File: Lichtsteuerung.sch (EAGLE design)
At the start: 132 parts, among them IC1 74HC595D, IC10 TSR_1-2450, IC11 MEGA64-A, IC12 75176AD, IC13 DS1307SO8, IC2 74HC595D, IC3 74HC595D, IC4 74HC595D, IC5 75176AD, IC6 MEGA8-AI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

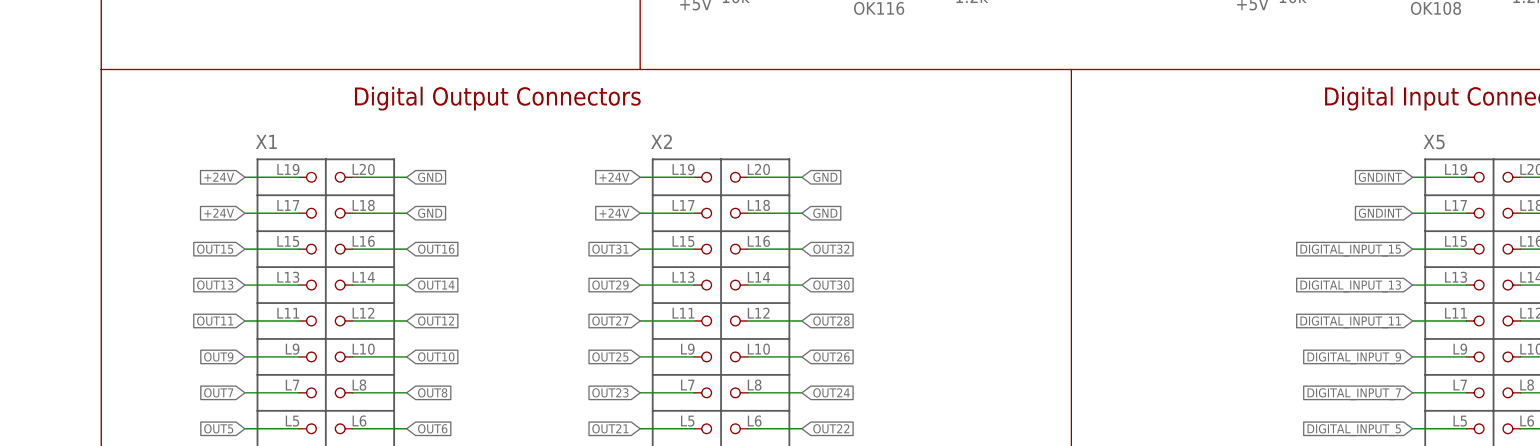
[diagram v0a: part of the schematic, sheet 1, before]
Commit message: Added polyfuses for the 24V rails
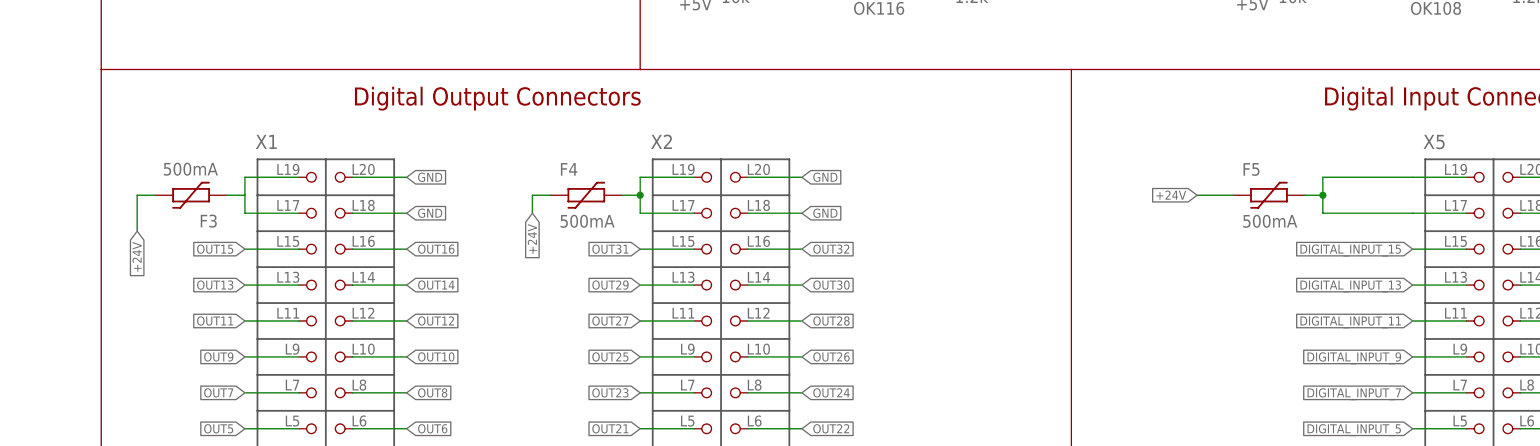
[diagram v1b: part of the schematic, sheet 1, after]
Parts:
- added F3, F4, F5: 500mA, ptc-littlefuse:1812L
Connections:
- new net +24V_01: F3.1, X1.L17, X1.L19
- new net +24V_02: F4.2, X2.L17, X2.L19
- new net +24V_03: F5.2, X5.L17, X5.L19
- net +24V: now also F3.2, F4.1, F5.1; no longer X1.L17, X1.L19, X2.L17, X2.L19
- net GNDINT: no longer X5.L17, X5.L19
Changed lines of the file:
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@@
 <part name="L2" library="epcos-b82790c0" deviceset="EPCOS_B82790C0" device="" value="2x51µH"/>
 <part name="JP3" library="pinhead" deviceset="PINHD-2X8" device=""/>
+<part name="F3" library="ptc-littlefuse" deviceset="1812L" device="" value="500mA"/>
+<part name="F4" library="ptc-littlefuse" deviceset="1812L" device="" value="500mA"/>
+<part name="F5" library="ptc-littlefuse" deviceset="1812L" device="" value="500mA"/>
 </parts>
 <sheets>
@@
 <instance part="P+26" gate="1" x="220.98" y="124.46" rot="R90"/>
 <instance part="P+27" gate="1" x="220.98" y="106.68" rot="R90"/>
+<instance part="F3" gate="G$1" x="152.4" y="76.2" rot="R180"/>
+<instance part="F4" gate="G$1" x="208.28" y="76.2"/>
+<instance part="F5" gate="G$1" x="304.8" y="76.2"/>
 </instances>
 <busses>
@@
 </segment>
 <segment>
-<wire x1="167.64" y1="78.74" x2="160.02" y2="78.74" width="0.1524" layer="91"/>
-<label x="160.02" y="78.74" size="1.27" layer="95" rot="R180" xref="yes"/>
-<pinref part="X1" gate="G$1" pin="L19"/>
-</segment>
-<segment>
-<wire x1="167.64" y1="73.66" x2="160.02" y2="73.66" width="0.1524" layer="91"/>
-<label x="160.02" y="73.66" size="1.27" layer="95" rot="R180" xref="yes"/>
-<pinref part="X1" gate="G$1" pin="L17"/>
-</segment>
-<segment>
-<wire x1="223.52" y1="78.74" x2="215.9" y2="78.74" width="0.1524" layer="91"/>
-<label x="215.9" y="78.74" size="1.27" layer="95" rot="R180" xref="yes"/>
-<pinref part="X2" gate="G$1" pin="L19"/>
-</segment>
-<segment>
-<wire x1="223.52" y1="73.66" x2="215.9" y2="73.66" width="0.1524" layer="91"/>
-<label x="215.9" y="73.66" size="1.27" layer="95" rot="R180" xref="yes"/>
-<pinref part="X2" gate="G$1" pin="L17"/>
+<pinref part="F5" gate="G$1" pin="1"/>
+<wire x1="299.72" y1="76.2" x2="294.64" y2="76.2" width="0.1524" layer="91"/>
+<label x="294.64" y="76.2" size="1.27" layer="95" rot="R180" xref="yes"/>
+</segment>
+<segment>
+<pinref part="F4" gate="G$1" pin="1"/>
+<wire x1="203.2" y1="76.2" x2="200.66" y2="76.2" width="0.1524" layer="91"/>
+<wire x1="200.66" y1="76.2" x2="200.66" y2="73.66" width="0.1524" layer="91"/>
+<label x="200.66" y="73.66" size="1.27" layer="95" rot="R270" xref="yes"/>
+</segment>
+<segment>
+<pinref part="F3" gate="G$1" pin="2"/>
+<wire x1="147.32" y1="76.2" x2="144.78" y2="76.2" width="0.1524" layer="91"/>
+<wire x1="144.78" y1="76.2" x2="144.78" y2="71.12" width="0.1524" layer="91"/>
+<label x="144.78" y="71.12" size="1.27" layer="95" rot="R270" xref="yes"/>
 </segment>
 </net>
@@
 </segment>
 <segment>
-<wire x1="332.74" y1="78.74" x2="325.12" y2="78.74" width="0.1524" layer="91"/>
-<label x="325.12" y="78.74" size="1.27" layer="95" rot="R180" xref="yes"/>
-<pinref part="X5" gate="G$1" pin="L19"/>
-</segment>
-<segment>
-<wire x1="332.74" y1="73.66" x2="325.12" y2="73.66" width="0.1524" layer="91"/>
-<label x="325.12" y="73.66" size="1.27" layer="95" rot="R180" xref="yes"/>
-<pinref part="X5" gate="G$1" pin="L17"/>
-</segment>
-<segment>
 <wire x1="340.36" y1="78.74" x2="347.98" y2="78.74" width="0.1524" layer="91"/>
 <label x="347.98" y="78.74" size="1.27" layer="95" xref="yes"/>
@@
 </segment>
 </net>
+<net name="+24V_01" class="1">
+<segment>
+<wire x1="167.64" y1="78.74" x2="160.02" y2="78.74" width="0.1524" layer="91"/>
+<pinref part="X1" gate="G$1" pin="L19"/>
+<wire x1="167.64" y1="73.66" x2="160.02" y2="73.66" width="0.1524" layer="91"/>
+<pinref part="X1" gate="G$1" pin="L17"/>
+<wire x1="160.02" y1="78.74" x2="160.02" y2="76.2" width="0.1524" layer="91"/>
+<wire x1="160.02" y1="76.2" x2="160.02" y2="73.66" width="0.1524" layer="91"/>
+<wire x1="160.02" y1="76.2" x2="157.48" y2="76.2" width="0.1524" layer="91"/>
+<pinref part="F3" gate="G$1" pin="1"/>
+</segment>
+</net>
+<net name="+24V_02" class="1">
+<segment>
+<wire x1="223.52" y1="78.74" x2="215.9" y2="78.74" width="0.1524" layer="91"/>
+<pinref part="X2" gate="G$1" pin="L19"/>
+<pinref part="F4" gate="G$1" pin="2"/>
+<wire x1="213.36" y1="76.2" x2="215.9" y2="76.2" width="0.1524" layer="91"/>
+<wire x1="215.9" y1="76.2" x2="215.9" y2="78.74" width="0.1524" layer="91"/>
+<wire x1="223.52" y1="73.66" x2="215.9" y2="73.66" width="0.1524" layer="91"/>
+<pinref part="X2" gate="G$1" pin="L17"/>
+<wire x1="215.9" y1="76.2" x2="215.9" y2="73.66" width="0.1524" layer="91"/>
+<junction x="215.9" y="76.2"/>
+</segment>
+</net>
+<net name="+24V_03" class="1">
+<segment>
+<wire x1="332.74" y1="78.74" x2="325.12" y2="78.74" width="0.1524" layer="91"/>
+<pinref part="X5" gate="G$1" pin="L19"/>
+<pinref part="F5" gate="G$1" pin="2"/>
+<wire x1="309.88" y1="76.2" x2="312.42" y2="76.2" width="0.1524" layer="91"/>
+<wire x1="312.42" y1="76.2" x2="312.42" y2="78.74" width="0.1524" layer="91"/>
+<wire x1="312.42" y1="78.74" x2="325.12" y2="78.74" width="0.1524" layer="91"/>
+<wire x1="312.42" y1="76.2" x2="312.42" y2="73.66" width="0.1524" layer="91"/>
+<wire x1="332.74" y1="73.66" x2="325.12" y2="73.66" width="0.1524" layer="91"/>
+<pinref part="X5" gate="G$1" pin="L17"/>
+<wire x1="312.42" y1="73.66" x2="325.12" y2="73.66" width="0.1524" layer="91"/>
+<junction x="312.42" y="76.2"/>
+</segment>
+</net>

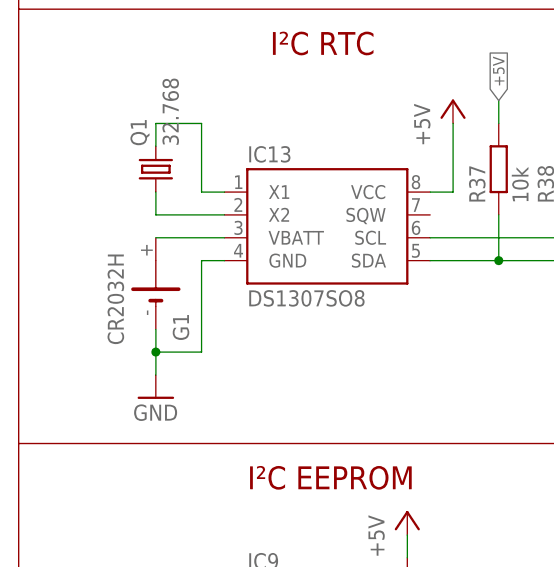
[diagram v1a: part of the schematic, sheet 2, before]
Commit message: Fixed wrong battery holder
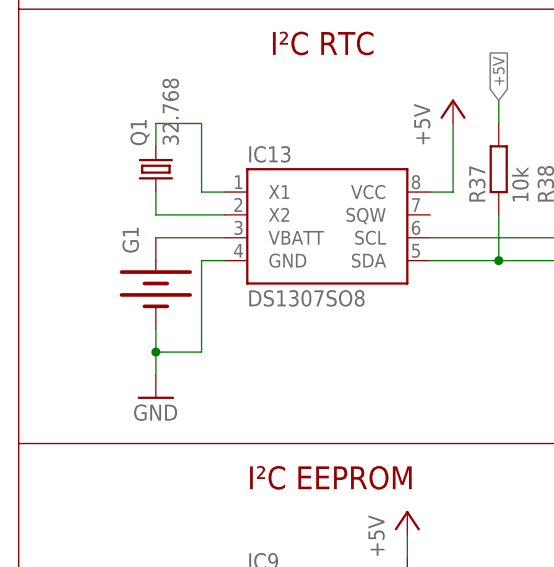
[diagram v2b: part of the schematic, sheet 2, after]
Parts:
- G1: value CR2032H -> (none); device battery:CR2032H -> SparkFun:BATTERY20PTH
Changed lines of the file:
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@@
 <part name="FRAME3" library="frames" deviceset="A3L-LOC" device=""/>
 <part name="IC13" library="SparkFun" deviceset="DS1307" device="SO8"/>
-<part name="G1" library="battery" deviceset="CR2032H" device=""/>
+<part name="G1" library="SparkFun" deviceset="BATTERY" device="20PTH"/>
 <part name="Q1" library="crystal" deviceset="MC-306" device="" value="32.768"/>
 <part name="R37" library="resistor" deviceset="R-EU_" device="R0805" value="10k"/>
@@
 <instance part="FRAME3" gate="G$1" x="0" y="0"/>
 <instance part="IC13" gate="G$1" x="43.18" y="147.32"/>
-<instance part="G1" gate="1" x="25.4" y="139.7" smashed="yes" rot="R90">
-<attribute name="NAME" x="27.305" y="136.398" size="1.778" layer="95" rot="R270"/>
-<attribute name="VALUE" x="21.844" y="132.842" size="1.778" layer="96" rot="R90"/>
+<instance part="G1" gate="G$1" x="25.4" y="139.7" smashed="yes" rot="R270">
+<attribute name="NAME" x="23.495" y="143.002" size="1.778" layer="95" rot="R90"/>
+<attribute name="VALUE" x="28.956" y="146.558" size="1.778" layer="96" rot="R270"/>
 </instance>
 <instance part="Q1" gate="P" x="25.4" y="152.4" rot="R90"/>
@@
 <segment>
 <wire x1="25.4" y1="144.78" x2="33.02" y2="144.78" width="0.1524" layer="91"/>
-<pinref part="G1" gate="1" pin="+"/>
+<pinref part="G1" gate="G$1" pin="+"/>
 <pinref part="IC13" gate="G$1" pin="VBATT"/>
 </segment>
@@
 <wire x1="25.4" y1="129.54" x2="25.4" y2="132.08" width="0.1524" layer="91"/>
 <junction x="25.4" y="132.08"/>
-<pinref part="G1" gate="1" pin="-"/>
+<pinref part="G1" gate="G$1" pin="-"/>
 <pinref part="IC13" gate="G$1" pin="GND"/>
 <pinref part="GND21" gate="1" pin="GND"/>

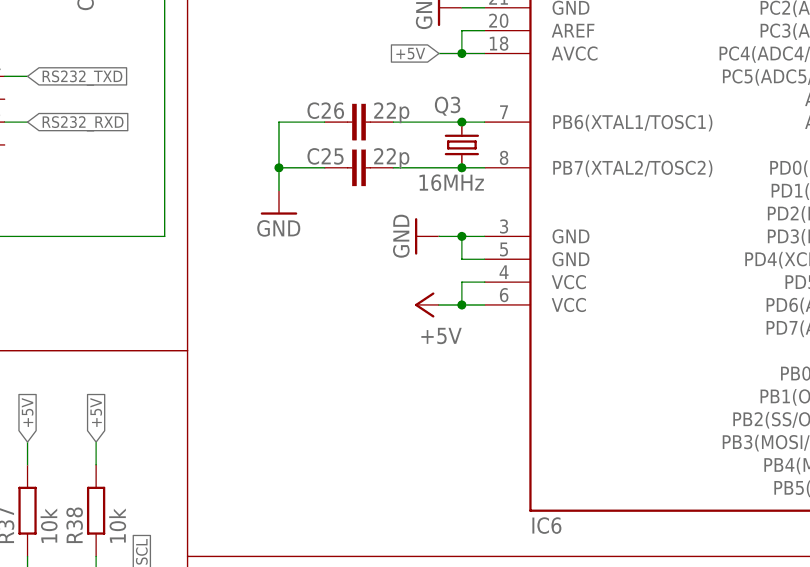
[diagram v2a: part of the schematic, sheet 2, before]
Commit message: Added missing bypass cap for the second avr
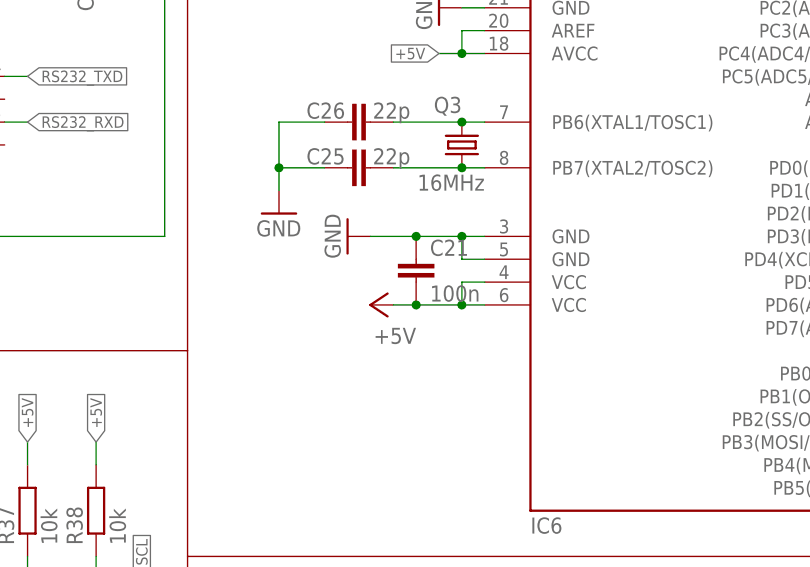
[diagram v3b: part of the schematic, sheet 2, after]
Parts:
- added C21: 100n, resistor:C-EUC0805
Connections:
- net +5V: now also C21.2
- net GND: now also C21.1
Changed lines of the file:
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@@
 <part name="F4" library="ptc-littlefuse" deviceset="1812L" device="" value="500mA"/>
 <part name="F5" library="ptc-littlefuse" deviceset="1812L" device="" value="500mA"/>
+<part name="C21" library="resistor" deviceset="C-EU" device="C0805" value="100n"/>
 </parts>
 <sheets>
@@
 <instance part="R40" gate="G$1" x="111.76" y="220.98" rot="R90"/>
 <instance part="P+18" gate="1" x="111.76" y="231.14"/>
-<instance part="GND30" gate="1" x="106.68" y="182.88" rot="R270"/>
-<instance part="P+20" gate="1" x="106.68" y="175.26" rot="R90"/>
+<instance part="GND30" gate="1" x="99.06" y="182.88" rot="R270"/>
+<instance part="P+20" gate="1" x="101.6" y="175.26" rot="R90"/>
 <instance part="GND31" gate="1" x="109.22" y="208.28" rot="R270"/>
 <instance part="X3" gate="G$1" x="246.38" y="78.74"/>
@@
 <attribute name="VALUE" x="347.472" y="157.48" size="1.778" layer="96" rot="MR180"/>
 </instance>
+<instance part="C21" gate="G$1" x="106.68" y="180.34"/>
 </instances>
 <busses>
@@
 </segment>
 <segment>
-<wire x1="109.22" y1="175.26" x2="111.76" y2="175.26" width="0.1524" layer="91"/>
+<wire x1="104.14" y1="175.26" x2="106.68" y2="175.26" width="0.1524" layer="91"/>
+<wire x1="106.68" y1="175.26" x2="111.76" y2="175.26" width="0.1524" layer="91"/>
 <wire x1="111.76" y1="175.26" x2="114.3" y2="175.26" width="0.1524" layer="91"/>
 <wire x1="114.3" y1="177.8" x2="111.76" y2="177.8" width="0.1524" layer="91"/>
@@
 <pinref part="IC6" gate="G$1" pin="VCC@2"/>
 <pinref part="IC6" gate="G$1" pin="VCC@1"/>
+<pinref part="C21" gate="G$1" pin="2"/>
+<junction x="106.68" y="175.26"/>
 </segment>
 <segment>
@@
 <wire x1="114.3" y1="180.34" x2="111.76" y2="180.34" width="0.1524" layer="91"/>
 <wire x1="111.76" y1="180.34" x2="111.76" y2="182.88" width="0.1524" layer="91"/>
-<wire x1="111.76" y1="182.88" x2="109.22" y2="182.88" width="0.1524" layer="91"/>
+<wire x1="111.76" y1="182.88" x2="106.68" y2="182.88" width="0.1524" layer="91"/>
 <junction x="111.76" y="182.88"/>
 <pinref part="IC6" gate="G$1" pin="GND@1"/>
 <pinref part="IC6" gate="G$1" pin="GND@2"/>
 <pinref part="GND30" gate="1" pin="GND"/>
-</segment>
-<segment>
+<pinref part="C21" gate="G$1" pin="1"/>
+<wire x1="106.68" y1="182.88" x2="101.6" y2="182.88" width="0.1524" layer="91"/>
+<junction x="106.68" y="182.88"/>
+</segment>
+<segment>

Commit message: Fixed serial eeprom footprint
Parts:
- IC9: device microchip:24AA256SN -> microchip:24AA01SM
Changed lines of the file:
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@@
 <part name="JP1" library="con-ml" deviceset="ML10" device=""/>
 <part name="R39" library="resistor" deviceset="R-EU_" device="R0805" value="10k"/>
-<part name="IC9" library="microchip" deviceset="24*" device="SN" technology="AA256" value="24FC128-I/SN"/>
+<part name="IC9" library="microchip" deviceset="24*" device="SM" technology="AA01" value="24FC128-I/SN"/>
 <part name="IC10" library="_traco_tsr-1" deviceset="TSR_1-*" device="" technology="2450"/>
 <part name="C9" library="rcl" deviceset="C-EU" device="C0805" value="1µ"/>

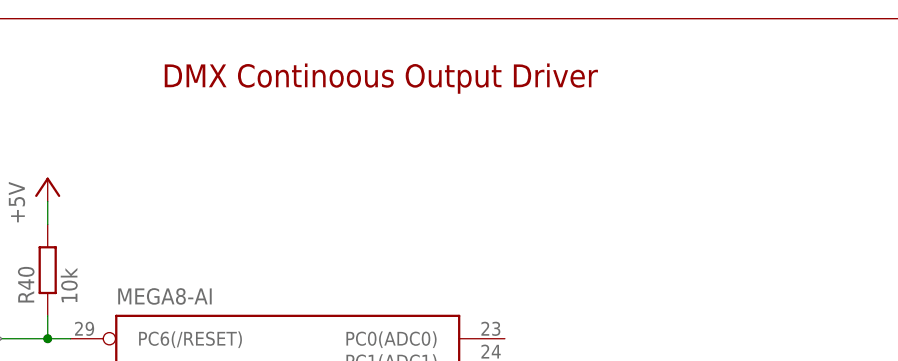
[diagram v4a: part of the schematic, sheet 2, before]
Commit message: Fixed typo
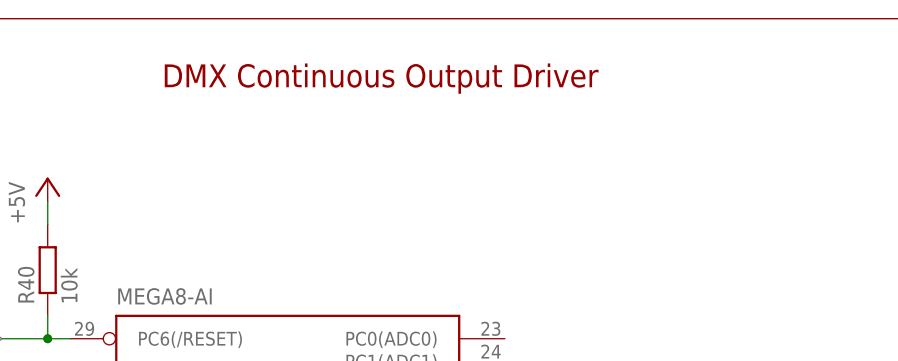
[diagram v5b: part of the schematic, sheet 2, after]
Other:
- note added: "DMX Continuous Output Driver"
- note removed: "DMX Continoous Output Driver"
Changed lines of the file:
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@@
 <text x="289.56" y="15.24" size="2.54" layer="94" font="vector">and Serial I/O</text>
 <text x="190.5" y="175.26" size="2.54" layer="94" font="vector">ISP for atmega8</text>
-<text x="124.46" y="241.3" size="2.54" layer="94" font="vector">DMX Continoous Output Driver</text>
+<text x="124.46" y="241.3" size="2.54" layer="94" font="vector">DMX Continuous Output Driver</text>
 <text x="228.6" y="96.52" size="1.778" layer="94" font="vector">DMX Input Connector</text>
 <text x="261.62" y="96.52" size="1.778" layer="94" font="vector">DMX Ouput Connector</text>
